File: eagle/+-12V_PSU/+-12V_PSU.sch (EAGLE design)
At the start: 23 parts, among them CN1 OUT, IC1 7812T, IC2 7912

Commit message: Add: +-12V_PSU eagle files
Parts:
- C1, C2: device rcl:CPOL-EUSANYO_C6 -> rcl:CPOL-EUE2.5-7
- C3, C4: device rcl:CPOL-EUE5-10.5 -> rcl:CPOL-EUE7.5-16
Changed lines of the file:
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@@
 <part name="IC2" library="linear" library_urn="urn:adsk.eagle:library:262" deviceset="79*" device="T" package3d_urn="urn:adsk.eagle:package:16414/1" technology="12" value="7912"/>
 <part name="IC1" library="linear" library_urn="urn:adsk.eagle:library:262" deviceset="78*" device="T" package3d_urn="urn:adsk.eagle:package:16414/1" technology="12"/>
-<part name="C1" library="rcl" library_urn="urn:adsk.eagle:library:334" deviceset="CPOL-EU" device="SANYO_C6" package3d_urn="urn:adsk.eagle:package:23444/1" value="100uF"/>
-<part name="C2" library="rcl" library_urn="urn:adsk.eagle:library:334" deviceset="CPOL-EU" device="SANYO_C6" package3d_urn="urn:adsk.eagle:package:23444/1" value="100uF"/>
-<part name="C3" library="rcl" library_urn="urn:adsk.eagle:library:334" deviceset="CPOL-EU" device="E5-10.5" package3d_urn="urn:adsk.eagle:package:23372/1" value="470uF"/>
-<part name="C4" library="rcl" library_urn="urn:adsk.eagle:library:334" deviceset="CPOL-EU" device="E5-10.5" package3d_urn="urn:adsk.eagle:package:23372/1" value="470uF"/>
+<part name="C1" library="rcl" library_urn="urn:adsk.eagle:library:334" deviceset="CPOL-EU" device="E2.5-7" package3d_urn="urn:adsk.eagle:package:23345/1" value="100uF"/>
+<part name="C2" library="rcl" library_urn="urn:adsk.eagle:library:334" deviceset="CPOL-EU" device="E2.5-7" package3d_urn="urn:adsk.eagle:package:23345/1" value="100uF"/>
+<part name="C3" library="rcl" library_urn="urn:adsk.eagle:library:334" deviceset="CPOL-EU" device="E7.5-16" package3d_urn="urn:adsk.eagle:package:23382/2" value="470uF"/>
+<part name="C4" library="rcl" library_urn="urn:adsk.eagle:library:334" deviceset="CPOL-EU" device="E7.5-16" package3d_urn="urn:adsk.eagle:package:23382/2" value="470uF"/>
 <part name="C5" library="rcl" library_urn="urn:adsk.eagle:library:334" deviceset="C-EU" device="025-024X044" package3d_urn="urn:adsk.eagle:package:23630/1" value="0.33uF"/>
 <part name="C6" library="rcl" library_urn="urn:adsk.eagle:library:334" deviceset="C-EU" device="025-024X044" package3d_urn="urn:adsk.eagle:package:23630/1" value="0.33uF"/>

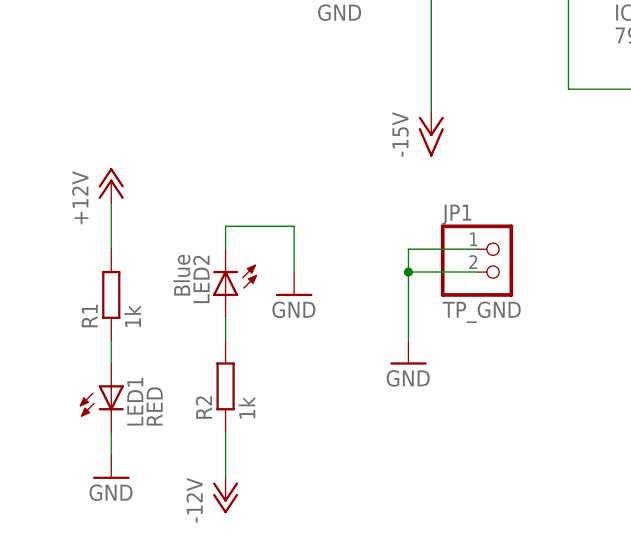
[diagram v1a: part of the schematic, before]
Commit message: +-12V_PSU Soldering Complete
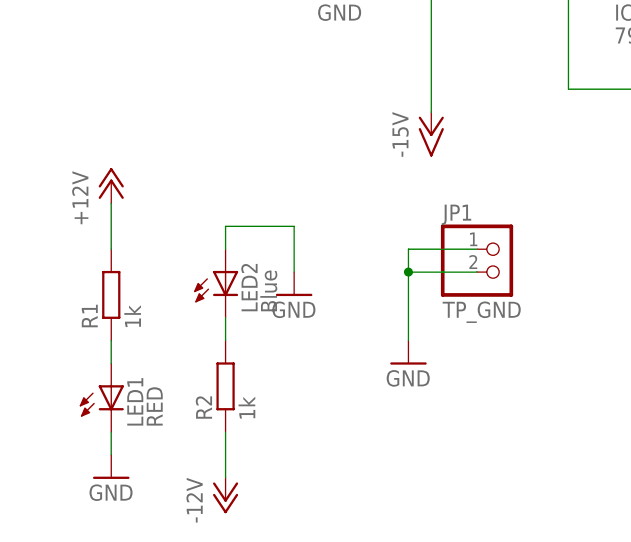
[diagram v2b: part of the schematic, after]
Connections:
- net GND: now also LED2.A; no longer LED2.C
- net N$3: now also LED2.C; no longer LED2.A
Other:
- moved on the sheet: LED2
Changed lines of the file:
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@@
 <instance part="CN1" gate="G$1" x="165.1" y="86.36" rot="R180"/>
 <instance part="LED1" gate="G$1" x="33.02" y="25.4"/>
-<instance part="LED2" gate="G$1" x="45.72" y="35.56" rot="R180"/>
+<instance part="LED2" gate="G$1" x="45.72" y="38.1"/>
 <instance part="R1" gate="G$1" x="33.02" y="35.56" rot="R90"/>
 <instance part="R2" gate="G$1" x="45.72" y="25.4" rot="R90"/>
@@
 <pinref part="GND4" gate="1" pin="GND"/>
 <wire x1="53.34" y1="43.18" x2="53.34" y2="38.1" width="0.1524" layer="91"/>
-<pinref part="LED2" gate="G$1" pin="C"/>
-<wire x1="45.72" y1="40.64" x2="45.72" y2="43.18" width="0.1524" layer="91"/>
+<pinref part="LED2" gate="G$1" pin="A"/>
+<wire x1="45.72" y1="43.18" x2="45.72" y2="40.64" width="0.1524" layer="91"/>
 </segment>
 <segment>
@@
 <segment>
 <pinref part="R2" gate="G$1" pin="2"/>
-<pinref part="LED2" gate="G$1" pin="A"/>
-<wire x1="45.72" y1="30.48" x2="45.72" y2="33.02" width="0.1524" layer="91"/>
-</segment>
-</net>
+<pinref part="LED2" gate="G$1" pin="C"/>
+<wire x1="45.72" y1="33.02" x2="45.72" y2="30.48" width="0.1524" layer="91"/>
+</segment>
+</net>
